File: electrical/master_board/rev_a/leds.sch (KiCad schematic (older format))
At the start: 52 parts, among them Q10 2N7000;SOT23, Q11 2N7000;SOT23, Q12 2N7000;SOT23, Q13 2N7000;SOT23, Q14 2N7000;SOT23, Q15 2N7000;SOT23, Q16 2N7000;SOT23, Q17 2N7000;SOT23, Q18 2N7000;SOT23, Q19 2N7000;SOT23, Q4 2N7000;SOT23, Q5 2N7000;SOT23, Q6 2N7000;SOT23, Q7 2N7000;SOT23, Q8 2N7000;SOT23, Q9 2N7000;SOT23, U11 SN74HCS595;TTSOP16, U12 SN74HCS595;TTSOP16

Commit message: Assigned PCB footprints.
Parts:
- C20, C21: footprint (none) -> Capacitor_SMD:C_0603_1608Metric
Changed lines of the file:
@@
 F 0 "C20" H 3600 7050 50  0000 L CNN
 F 1 "10pF;1608" H 3850 6850 50  0000 L CNN
-F 2 "" H 3838 6800 50  0001 C CNN
+F 2 "Capacitor_SMD:C_0603_1608Metric" H 3838 6800 50  0001 C CNN
 F 3 "~" H 3800 6950 50  0001 C CNN
 	1    3800 6950
@@
 F 0 "C21" H 4200 7050 50  0000 L CNN
 F 1 "10pF;1608" H 4450 6850 50  0000 L CNN
-F 2 "" H 4438 6800 50  0001 C CNN
+F 2 "Capacitor_SMD:C_0603_1608Metric" H 4438 6800 50  0001 C CNN
 F 3 "~" H 4400 6950 50  0001 C CNN
 	1    4400 6950

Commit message: More work thinning rats nest of unconnected wires.
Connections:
- net labels removed: LED8_TO_LED9
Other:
- note added: "TO DO:\n1. Add test points."
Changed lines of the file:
@@
 	3100 5900 4100 5900
 Text Label 2100 3700 0    50   ~ 0
-LED8_TO_LED9
+LED8
 Text Label 3400 2500 2    50   ~ 0
 LED11
@@
 Entry Wire Line
 	3500 1400 3600 1300
-Entry Wire Line
-	3950 1000 4050 1100
 Wire Wire Line
 	1000 1300 3400 1300
@@
 	3600 7200 3800 7200
 Connection ~ 3800 7200
+Text Notes 4400 850  0    80   ~ 0
+TO DO:\n1. Add test points.
 Wire Bus Line
 	3500 1300 3500 7200

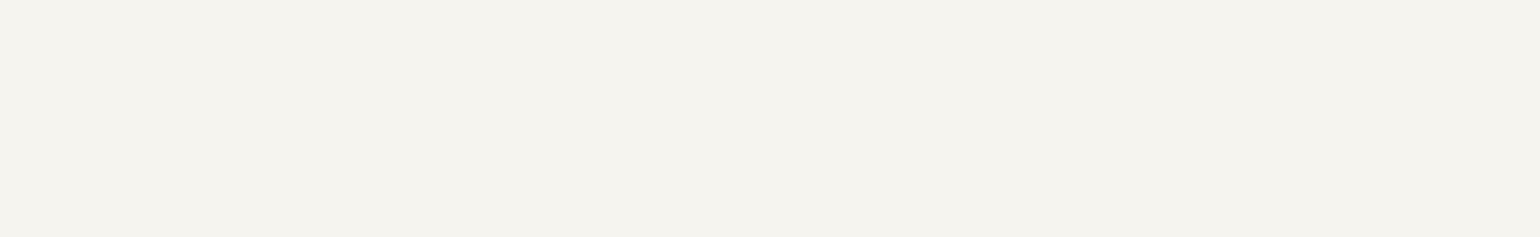
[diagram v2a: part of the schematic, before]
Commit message: Added test points and shunts to power supply.
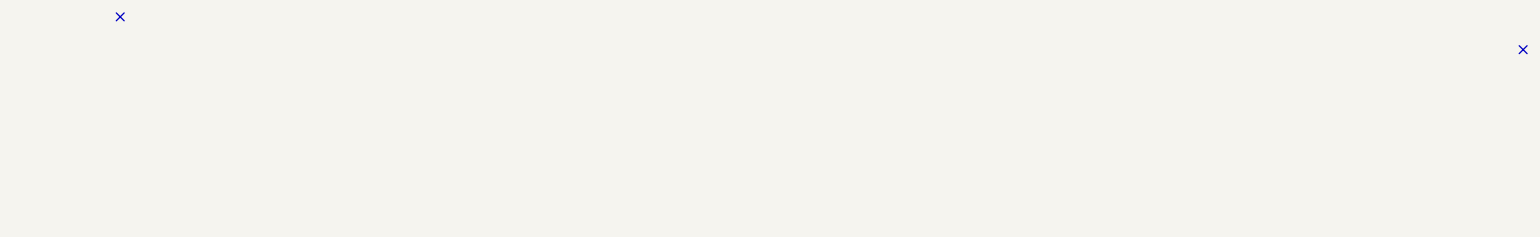
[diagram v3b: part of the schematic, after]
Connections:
- no-connect marks 2 -> 4
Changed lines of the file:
@@
 Text Notes 4400 850  0    80   ~ 0
 TO DO:\n1. Add test points.
+NoConn ~ 3050 -850
+NoConn ~ 11600 -650
 Wire Bus Line
 	3500 1300 3500 7200

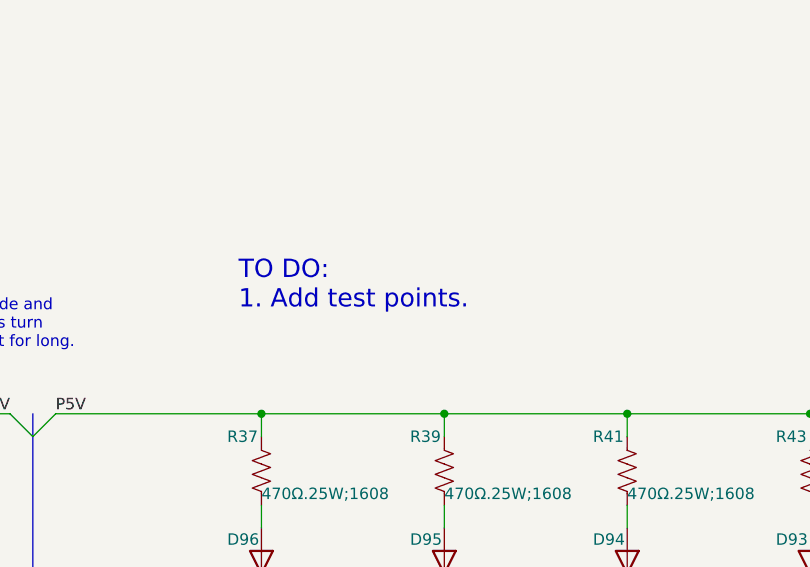
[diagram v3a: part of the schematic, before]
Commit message: Pin reassignments to support servo current.
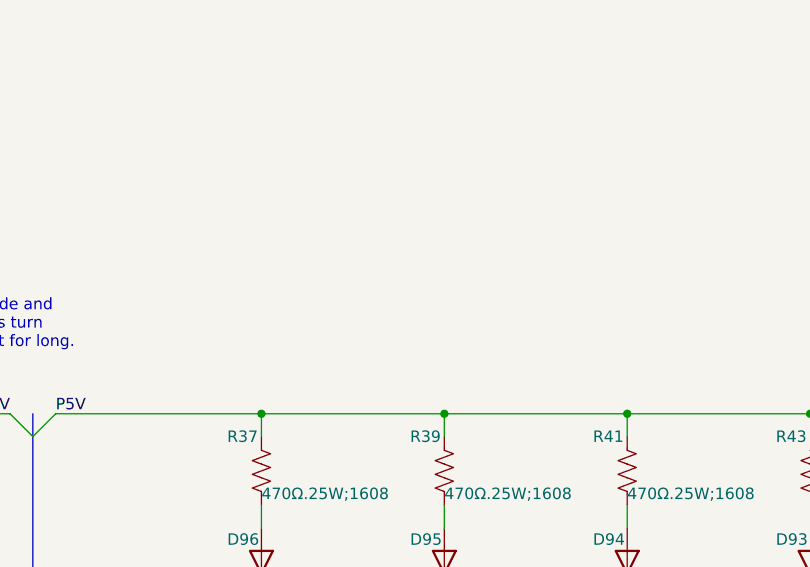
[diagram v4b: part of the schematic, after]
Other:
- note removed: "TO DO:\n1. Add test points."
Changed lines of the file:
@@
 	3600 7200 3800 7200
 Connection ~ 3800 7200
-Text Notes 4400 850  0    80   ~ 0
-TO DO:\n1. Add test points.
 NoConn ~ 3050 -850
 NoConn ~ 11600 -650
